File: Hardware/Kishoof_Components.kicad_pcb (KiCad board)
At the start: 4 copper layers, 70.8 x 110 mm, 113 parts, among them J1 SWD_Header, J10 VOct, J11 WavetablePosA, J12 WavetablePos, J13 VCA, J14 Conn_01x02_Socket, J15 Conn_01x02_Socket, J16 Conn_01x02_Socket, J17 Conn_01x02_Socket, J18 USB_C_Receptacle, J2 Eurorack_10_pin_power, J4 Conn_01x01_Socket, J7 Audio_Out_L, J8 Audio_Out_R, J9 WarpCV, SW1 Encoder, SW2 Mode_Switch, SW3 Octave_Switch, SW4 ChB_Output, SW5 SW_Push, U1 STM32H7B0VBTx, U2 PCM5100APW, U3 TPS561201, U4 LT1117-3.3, U5 MCP6002, U6 MX25LM51245G, U7 MCP6004, U8 TL072, U9 STF202-22T1G, Y1 8MHz 20pF

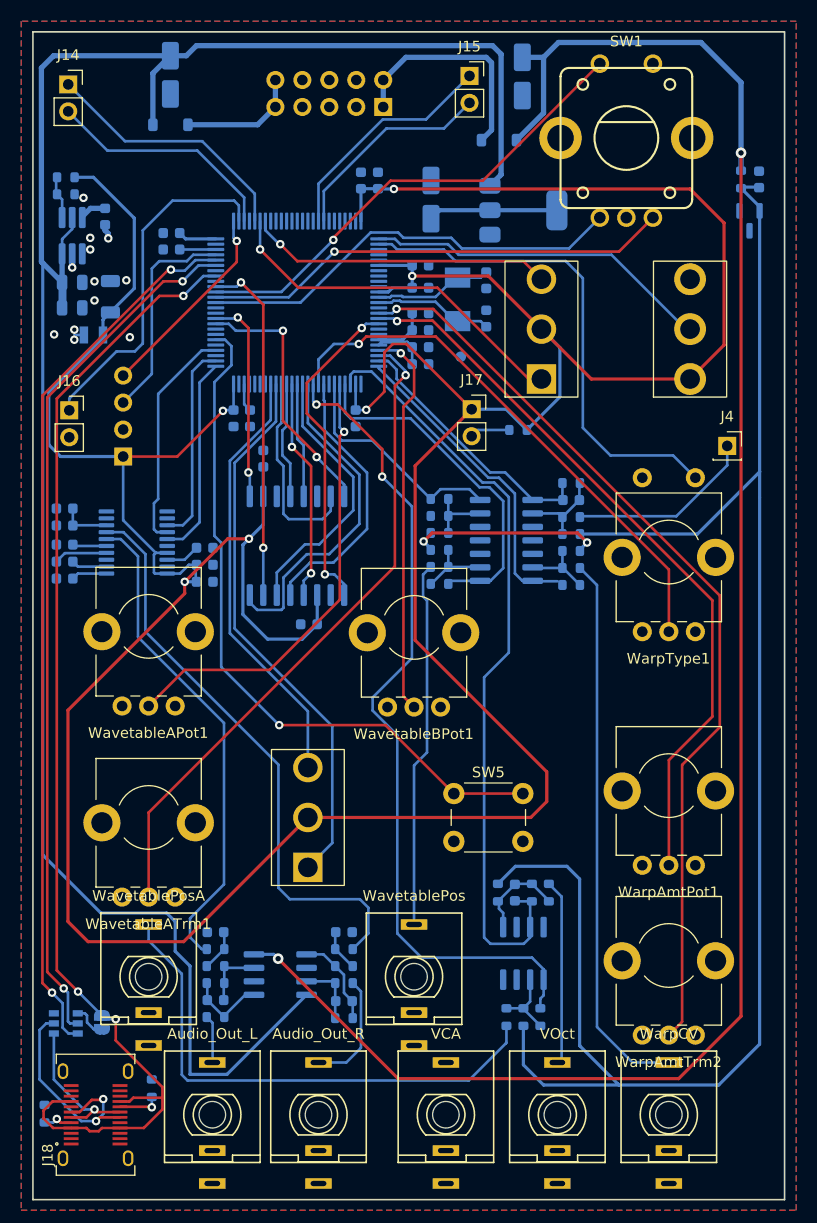
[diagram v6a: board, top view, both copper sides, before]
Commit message: Added LCD Riser board; power routing
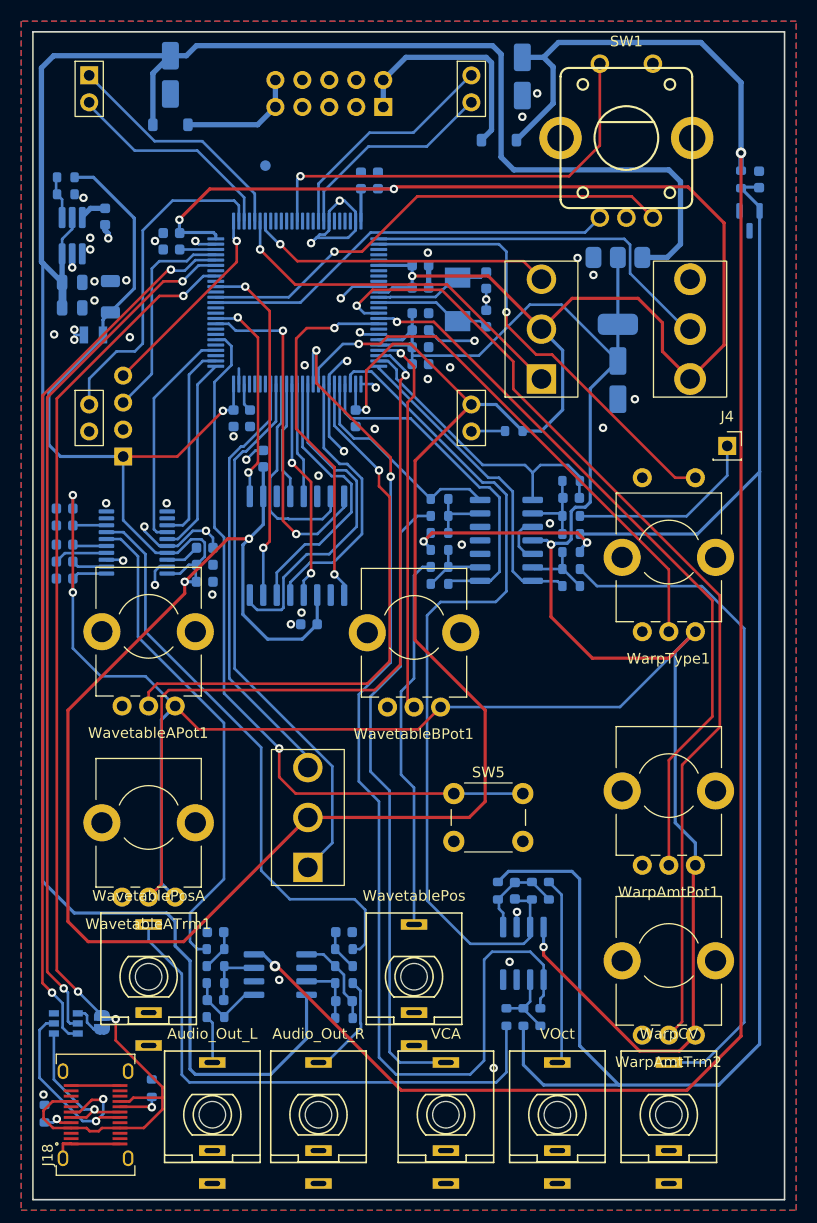
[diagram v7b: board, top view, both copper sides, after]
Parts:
- removed J14, J15, J16, J17: Conn_01x02_Socket, Connector_PinSocket_2.54mm:PinSocket_1x02_P2.54mm_Vertical
- added U10: ~, Custom_Footprints:LCD_Riser, F.Cu at (60.4, 43.1)
- moved TP1 25.7 mm to (77.0, 51.6)
- moved C5 24.5 mm to (110.2, 71.8), turned to -90 degrees
- moved U4 11.7 mm to (110.2, 63.4), turned to -90 degrees
- moved R15 0.41 mm to (100.4, 76.6)
- moved R34 0.20 mm to (105.8, 81.3), turned to 180 degrees
- moved C37 0.20 mm to (105.8, 82.9), turned to 180 degrees
- moved C35 0.17 mm to (100.5, 119.9)
- moved R22 0.17 mm to (98.9, 119.9)
- moved R23 0.17 mm to (103.7, 119.9)
- moved R24 0.17 mm to (102.1, 119.9)
- moved R13 0.10 mm to (105.8, 91.2)
- moved R33 0.10 mm to (105.8, 84.6)
- moved R18 0.10 mm to (105.8, 88.0)
- moved R20 0.10 mm to (105.8, 89.6)
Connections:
- U1 pad 30: /WAVETABLE_POS_A_POT -> /VcaCV
- U1 pad 31: /VcaCV -> /WAVETABLE_POS_A_POT
- U1 pad 32: unconnected-(U1-PC4-Pad32) -> GND
- U1 pad 65: /ENCODER_BTN -> unconnected-(U1-PC8-Pad65)
- U1 pad 88: unconnected-(U1-PD7-Pad88) -> /ENCODER_BTN
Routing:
- net +3.3VA: track 31.0 -> 262.4 mm, vias 0 -> 4
- net GND: track 0.00 -> 76.4 mm, vias 8 -> 49
- net /VCA_CV: track 0.00 -> 60.0 mm
- net +12V: track 194.0 -> 222.3 mm
- net /WavetablePosA_CV: track 78.2 -> 106.1 mm
- net +3.3V: track 376.8 -> 399.7 mm, vias 6 -> 7
- net /WARP_CV: track 52.1 -> 63.6 mm
- net /WAVETABLE_POS_A_TRM: track 62.7 -> 74.1 mm
- net /WAVETABLE_POS_A_POT: track 42.8 -> 53.5 mm
- net /Pitch_CV_Scaled: track 73.1 -> 81.8 mm
- net /OCTOSPIM_P1_IO1: track 24.6 -> 32.9 mm
- net /WARP_AMT_TRM: track 86.9 -> 94.0 mm
- net /AudioIn: track 24.9 -> 29.1 mm
- net /Warp_Polarity_Btn: track 47.2 -> 43.0 mm, vias 0 -> 1
- net /ENCODER_BTN: track 45.2 -> 41.5 mm
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
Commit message: Added STM32H7B0 project for testing
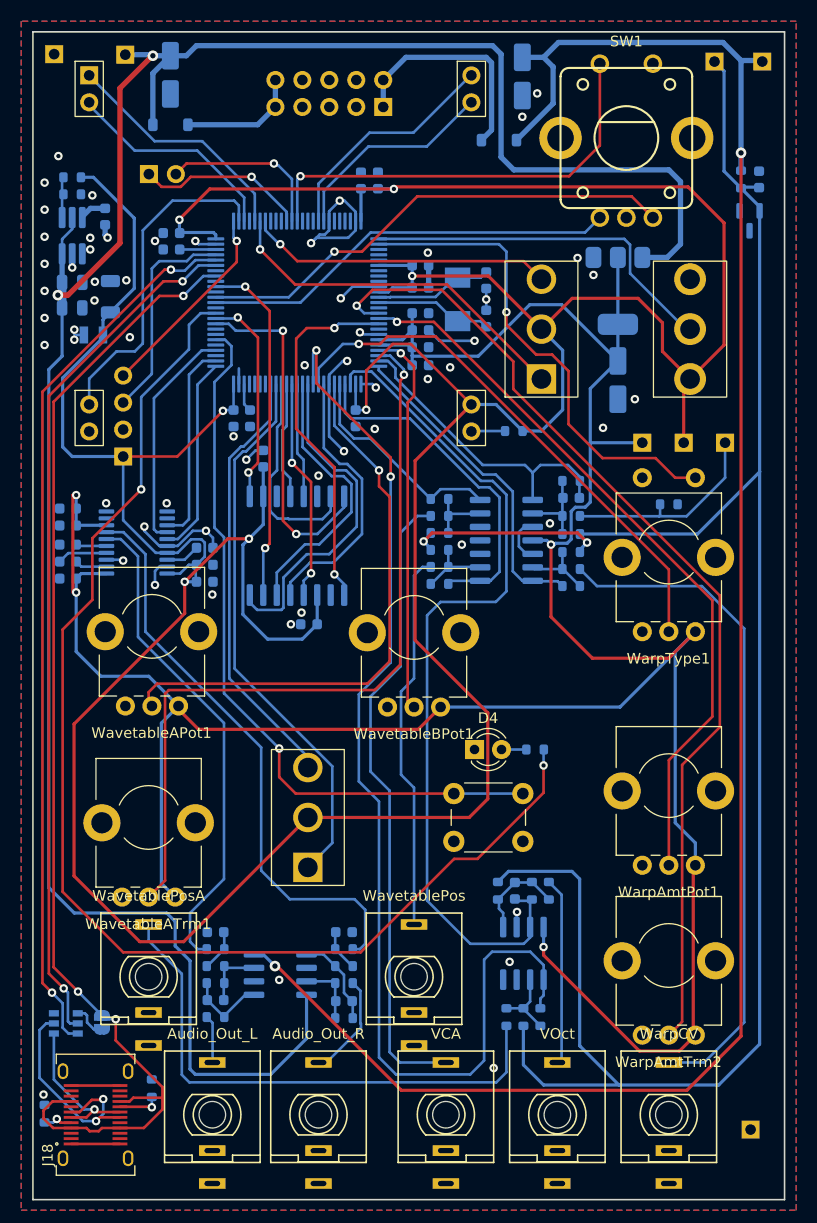
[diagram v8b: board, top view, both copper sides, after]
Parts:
- removed TP1: TestPoint, TestPoint:TestPoint_Pad_D1.0mm
- added D4: LED_Small, LED_THT:LED_D3.0mm_FlatTop, F.Cu at (96.7, 106.6)
- added J3: Conn_01x02_Pin, Connector_PinHeader_2.54mm:PinHeader_1x02_P2.54mm_Vertical, B.Cu at (66.0, 52.4)
- added R30: 1k, Resistor_SMD:R_0603_1608Metric, B.Cu at (102.4, 106.6)
- added R31: 100k, Resistor_SMD:R_0603_1608Metric, B.Cu at (115.0, 83.5)
- added TP2: TestPoint, Connector_PinSocket_2.54mm:PinSocket_1x01_P2.54mm_Vertical, B.Cu at (63.8, 41.1)
- added TP3: TestPoint, Connector_PinSocket_2.54mm:PinSocket_1x01_P2.54mm_Vertical, B.Cu at (123.8, 41.8)
- added TP4: TestPoint, Connector_PinSocket_2.54mm:PinSocket_1x01_P2.54mm_Vertical, B.Cu at (122.7, 142.4)
- added TP5: TestPoint, Connector_PinSocket_2.54mm:PinSocket_1x01_P2.54mm_Vertical, B.Cu at (116.4, 77.7)
- added TP6: TestPoint, Connector_PinSocket_2.54mm:PinSocket_1x01_P2.54mm_Vertical, B.Cu at (112.5, 77.7)
- added TP7: TestPoint, Connector_PinSocket_2.54mm:PinSocket_1x01_P2.54mm_Vertical, B.Cu at (119.3, 41.8)
- added TP8: TestPoint, Connector_PinSocket_2.54mm:PinSocket_1x01_P2.54mm_Vertical, B.Cu at (57.1, 41.1)
- J4: footprint Connector_PinSocket_2.54mm:PinSocket_1x01_P2.54mm_Vertical -> Connector_PinHeader_2.54mm:PinHeader_1x01_P2.54mm_Vertical; moved to B.Cu
- moved R1 0.60 mm to (58.8, 52.7)
- moved R2 0.60 mm to (58.8, 54.3)
- moved J4 0.36 mm to (120.3, 77.7), turned to 180 degrees
- moved C10 0.31 mm to (58.4, 90.5)
- moved C11 0.31 mm to (58.4, 85.5)
- moved C12 0.31 mm to (58.4, 83.9)
- moved C25 0.31 mm to (58.4, 88.9)
- moved C26 0.31 mm to (58.4, 87.3)
- moved WavetableAPot1 0.31 mm to (66.3, 95.0)
- moved C24 0.10 mm to (91.6, 70.4)
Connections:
- net /B_Octave_Btn1 renamed /B_Octave_Btn
- U1 pad 14: /RESET -> unconnected-(U1-NRST-Pad14)
- U1 pad 61: unconnected-(U1-PD14-Pad61) -> /LED_B_Oct
- U1 pad 86: unconnected-(U1-PD5-Pad86) -> /UART_TX
- U1 pad 87: unconnected-(U1-PD6-Pad87) -> /UART_RX
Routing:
- net /LED_B_Oct: track 0.00 -> 119.3 mm, vias 0 -> 2
- net /UART_TX: track 0.00 -> 16.1 mm, vias 0 -> 1
- net /UART_RX: track 0.00 -> 15.9 mm, vias 0 -> 1
- net /-5V_REF: track 180.8 -> 193.8 mm
- net +12V: track 222.3 -> 215.8 mm, vias 0 -> 2
- net +3.3VA: track 262.4 -> 267.0 mm
- net -12V: track 177.1 -> 180.4 mm
- net /Warp_Polarity_Btn: track 43.0 -> 45.9 mm
- net /LED_OCT_B: track 0.00 -> 2.31 mm
- net GND: track 76.4 -> 74.2 mm, vias 49 -> 56
- net /EXT_AUDIO_IN: track 18.3 -> 19.6 mm
- net +3.3V: track 399.7 -> 400.5 mm
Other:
- board text added: "-12V"
- board text added: "-5V"
- board text added: "12V"
- board text added: "3V"
- board text added: "3VA"
- board text added: "Ext"
- board text added: "GND"
- board text added: "RX"
- board text added: "TX"
